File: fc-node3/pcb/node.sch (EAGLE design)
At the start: 22 parts, among them IC1 HTU21D, J1 AVR_SPI_PRG_62X3_LOCK, U1 DS18B20

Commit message: routed fc3
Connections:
- removed net DIO0: U$1.(PCINT1/AIN0/ADC1)PA1, U$4.DIO0
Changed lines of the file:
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@@
-</segment>
-</net>
-<net name="DIO0" class="0">
-<segment>
-<pinref part="U$4" gate="A" pin="DIO0"/>
-<wire x1="152.4" y1="48.26" x2="149.86" y2="48.26" width="0.1524" layer="91"/>
-<label x="149.86" y="48.26" size="1.27" layer="95" rot="R180" xref="yes"/>
-</segment>
-<segment>
-<pinref part="U$1" gate="G$1" pin="(PCINT1/AIN0/ADC1)PA1"/>
-<wire x1="45.72" y1="-58.42" x2="48.26" y2="-58.42" width="0.1524" layer="91"/>
-<label x="48.26" y="-58.42" size="1.27" layer="95" xref="yes"/>
 </segment>
 </net>

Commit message: nicey silky
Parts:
- renumbered U$2 to U2, U$3 to U3
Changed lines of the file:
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@@
 <part name="SUPPLY1" library="SparkFun-Aesthetics" deviceset="VCC" device=""/>
 <part name="GND1" library="SparkFun-Aesthetics" deviceset="GND" device=""/>
-<part name="U$2" library="ukhas" deviceset="MCP1640" device=""/>
-<part name="U$3" library="jonsowman" deviceset="BU49X_VDET_SOT235" device=""/>
+<part name="U2" library="ukhas" deviceset="MCP1640" device=""/>
+<part name="U3" library="jonsowman" deviceset="BU49X_VDET_SOT235" device=""/>
 <part name="GND2" library="SparkFun-Aesthetics" deviceset="GND" device=""/>
 <part name="GND3" library="SparkFun-Aesthetics" deviceset="GND" device=""/>
@@
 <instance part="SUPPLY1" gate="G$1" x="-7.62" y="-27.94"/>
 <instance part="GND1" gate="1" x="-7.62" y="-66.04"/>
-<instance part="U$2" gate="G$1" x="101.6" y="43.18"/>
-<instance part="U$3" gate="G$1" x="0" y="43.18"/>
+<instance part="U2" gate="G$1" x="101.6" y="43.18"/>
+<instance part="U3" gate="G$1" x="0" y="43.18"/>
 <instance part="GND2" gate="1" x="0" y="25.4"/>
 <instance part="GND3" gate="1" x="101.6" y="25.4"/>
@@
 <net name="GND" class="0">
 <segment>
-<pinref part="U$3" gate="G$1" pin="GND"/>
+<pinref part="U3" gate="G$1" pin="GND"/>
 <pinref part="GND2" gate="1" pin="GND"/>
 </segment>
 <segment>
-<pinref part="U$2" gate="G$1" pin="GND"/>
+<pinref part="U2" gate="G$1" pin="GND"/>
 <pinref part="GND3" gate="1" pin="GND"/>
 <pinref part="R2" gate="G$1" pin="1"/>
@@
 <net name="VCC" class="0">
 <segment>
-<pinref part="U$3" gate="G$1" pin="VDD"/>
+<pinref part="U3" gate="G$1" pin="VDD"/>
 <pinref part="SUPPLY2" gate="G$1" pin="VCC"/>
 </segment>
@@
 <pinref part="SUPPLY3" gate="G$1" pin="VCC"/>
 <wire x1="127" y1="50.8" x2="127" y2="48.26" width="0.1524" layer="91"/>
-<pinref part="U$2" gate="G$1" pin="VOUT"/>
+<pinref part="U2" gate="G$1" pin="VOUT"/>
 <wire x1="127" y1="48.26" x2="116.84" y2="48.26" width="0.1524" layer="91"/>
 <pinref part="R1" gate="G$1" pin="2"/>
@@
 <segment>
 <pinref part="DF" gate="G$1" pin="P$2"/>
-<pinref part="U$2" gate="G$1" pin="SW"/>
+<pinref part="U2" gate="G$1" pin="SW"/>
 <wire x1="96.52" y1="60.96" x2="101.6" y2="60.96" width="0.1524" layer="91"/>
 <wire x1="101.6" y1="60.96" x2="101.6" y2="58.42" width="0.1524" layer="91"/>
@@
 <wire x1="73.66" y1="40.64" x2="81.28" y2="40.64" width="0.1524" layer="91"/>
 <wire x1="81.28" y1="40.64" x2="81.28" y2="43.18" width="0.1524" layer="91"/>
-<pinref part="U$2" gate="G$1" pin="EN"/>
+<pinref part="U2" gate="G$1" pin="EN"/>
 <wire x1="81.28" y1="43.18" x2="86.36" y2="43.18" width="0.1524" layer="91"/>
 <pinref part="R3" gate="G$1" pin="1"/>
@@
 <pinref part="R1" gate="G$1" pin="1"/>
 <pinref part="R2" gate="G$1" pin="2"/>
-<pinref part="U$2" gate="G$1" pin="FB"/>
+<pinref part="U2" gate="G$1" pin="FB"/>
 <wire x1="116.84" y1="43.18" x2="116.84" y2="38.1" width="0.1524" layer="91"/>
 <wire x1="116.84" y1="38.1" x2="127" y2="38.1" width="0.1524" layer="91"/>
@@
 <wire x1="86.36" y1="60.96" x2="83.82" y2="60.96" width="0.1524" layer="91"/>
 <wire x1="83.82" y1="60.96" x2="83.82" y2="53.34" width="0.1524" layer="91"/>
-<pinref part="U$2" gate="G$1" pin="VIN"/>
+<pinref part="U2" gate="G$1" pin="VIN"/>
 <wire x1="83.82" y1="53.34" x2="83.82" y2="48.26" width="0.1524" layer="91"/>
 <wire x1="83.82" y1="48.26" x2="86.36" y2="48.26" width="0.1524" layer="91"/>
@@
 </segment>
 <segment>
-<pinref part="U$3" gate="G$1" pin="DETECT"/>
+<pinref part="U3" gate="G$1" pin="DETECT"/>
 <wire x1="12.7" y1="43.18" x2="15.24" y2="43.18" width="0.1524" layer="91"/>
 <label x="15.24" y="43.18" size="1.27" layer="95" xref="yes"/>

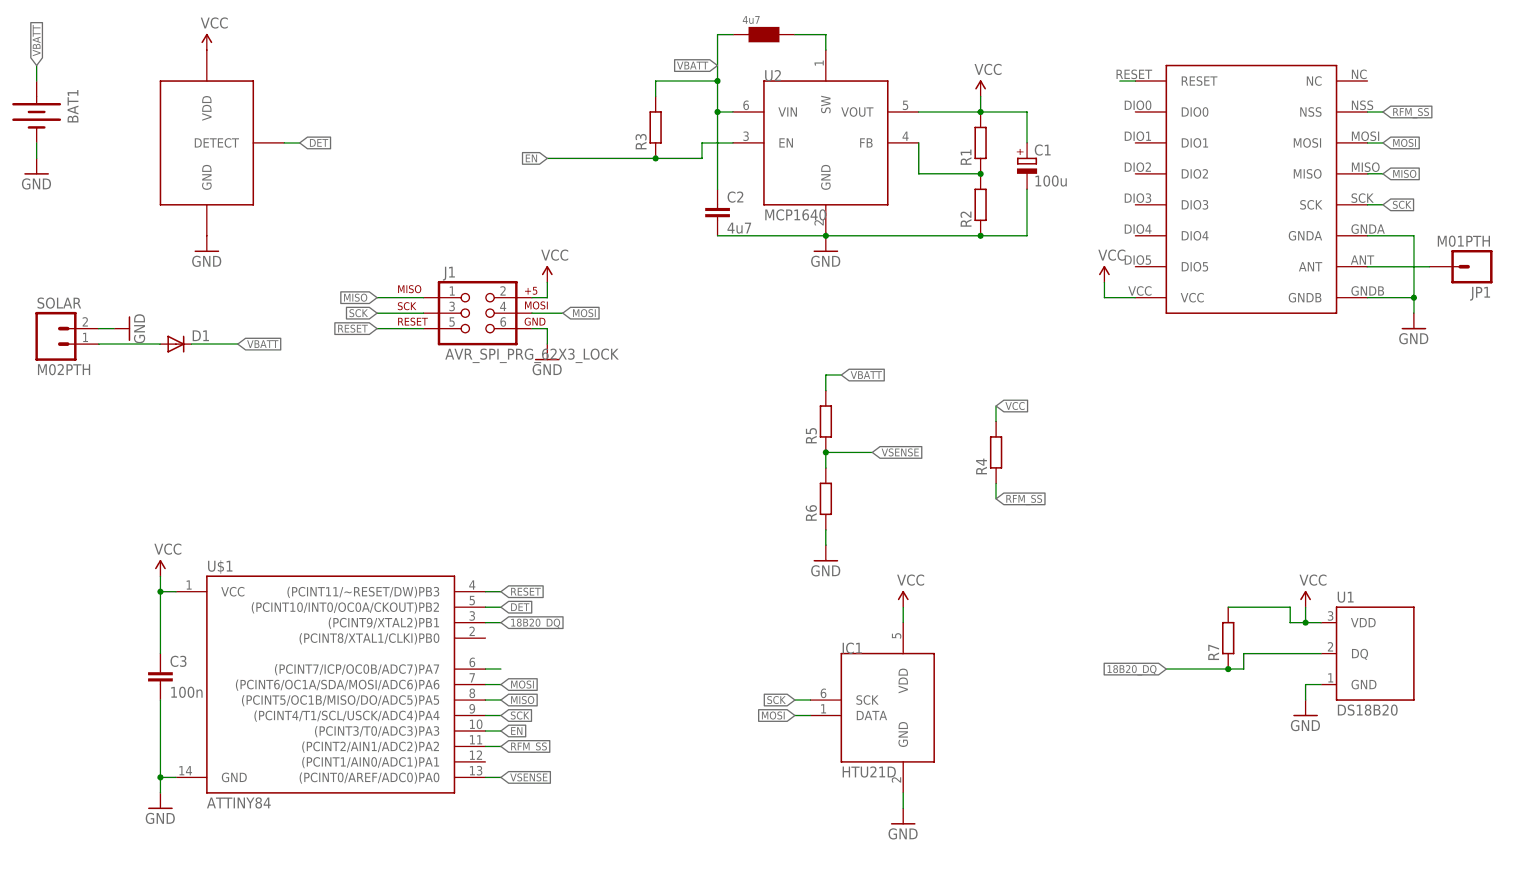
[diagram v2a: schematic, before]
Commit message: tidying routing for fc3
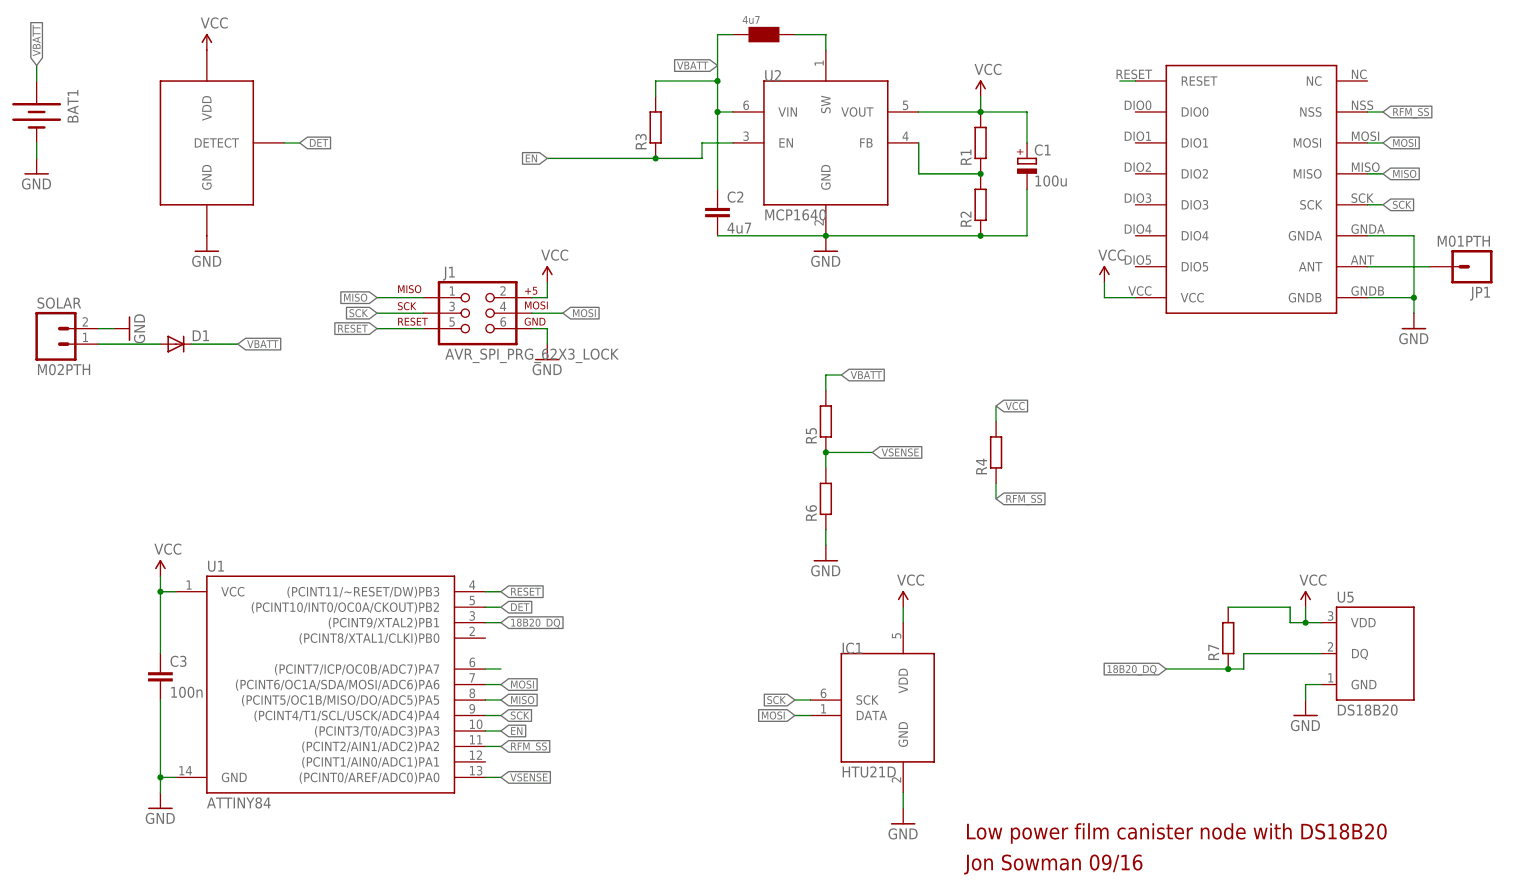
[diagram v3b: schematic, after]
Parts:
- removed U$1: ATTINY84, SparkFun-DigitalIC:ATTINY84
- added U5: DS18B20, SparkFun-Sensors:DS18B20
- U1: value DS18B20 -> ATTINY84; device SparkFun-Sensors:DS18B20 -> SparkFun-DigitalIC:ATTINY84
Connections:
- net 18B20_DQ: now also U1.(PCINT9/XTAL2)PB1, U5.DQ; no longer U$1.(PCINT9/XTAL2)PB1, U1.DQ
- net DET: now also U1.(PCINT10/INT0/OC0A/CKOUT)PB2; no longer U$1.(PCINT10/INT0/OC0A/CKOUT)PB2
- net EN: now also U1.(PCINT3/T0/ADC3)PA3; no longer U$1.(PCINT3/T0/ADC3)PA3
- net GND: now also U5.GND; no longer U$1.GND
- net MISO: now also U1.(PCINT5/OC1B/MISO/DO/ADC5)PA5; no longer U$1.(PCINT5/OC1B/MISO/DO/ADC5)PA5
- net MOSI: now also U1.(PCINT6/OC1A/SDA/MOSI/ADC6)PA6; no longer U$1.(PCINT6/OC1A/SDA/MOSI/ADC6)PA6
- net N$6: now also U1.(PCINT7/ICP/OC0B/ADC7)PA7; no longer U$1.(PCINT7/ICP/OC0B/ADC7)PA7
- net RESET: now also U1.(PCINT11/~RESET/DW)PB3; no longer U$1.(PCINT11/~RESET/DW)PB3
- net RFM_SS: now also U1.(PCINT2/AIN1/ADC2)PA2; no longer U$1.(PCINT2/AIN1/ADC2)PA2
- net SCK: now also U1.(PCINT4/T1/SCL/USCK/ADC4)PA4; no longer U$1.(PCINT4/T1/SCL/USCK/ADC4)PA4
- net VCC: now also U1.VCC, U5.VDD; no longer U$1.VCC, U1.VDD
- net VSENSE: now also U1.(PCINT0/AREF/ADC0)PA0; no longer U$1.(PCINT0/AREF/ADC0)PA0
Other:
- note added: "Jon Sowman 09/16"
- note added: "Low power film canister node with DS18B20"

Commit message: power ds18b20 from avr pin
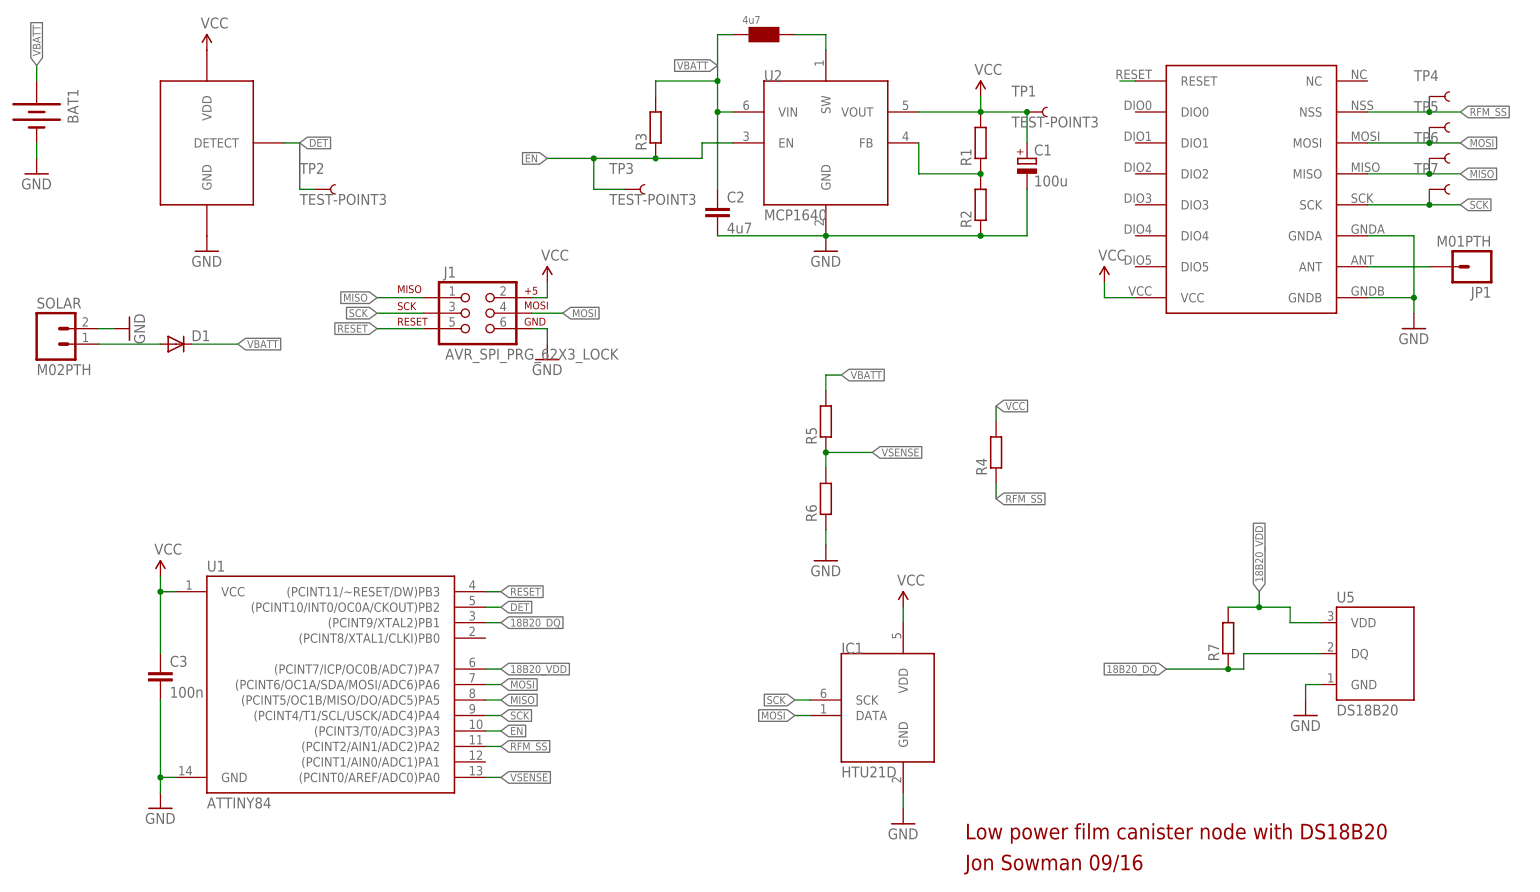
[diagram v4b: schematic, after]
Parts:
- added TP1, TP2, TP3, TP4, TP5, TP6, TP7: TEST-POINT3, SparkFun-Passives:TEST-POINT3
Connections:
- removed net N$6: U1.(PCINT7/ICP/OC0B/ADC7)PA7
- new net 18B20_VDD: R7.2, U1.(PCINT7/ICP/OC0B/ADC7)PA7, U5.VDD
- net DET: now also TP2.1
- net EN: now also TP3.1
- net MISO: now also TP6.1
- net MOSI: now also TP5.1
- net RFM_SS: now also TP4.1
- net SCK: now also TP7.1
- net VCC: now also TP1.1; no longer R7.2, U5.VDD
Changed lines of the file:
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@@
 <part name="R7" library="rcl" deviceset="R-EU_" device="R0603"/>
 <part name="GND10" library="SparkFun-Aesthetics" deviceset="GND" device=""/>
-<part name="SUPPLY7" library="SparkFun-Aesthetics" deviceset="VCC" device=""/>
+<part name="TP1" library="SparkFun-Passives" deviceset="TEST-POINT" device="3"/>
+<part name="TP2" library="SparkFun-Passives" deviceset="TEST-POINT" device="3"/>
+<part name="TP3" library="SparkFun-Passives" deviceset="TEST-POINT" device="3"/>
+<part name="TP4" library="SparkFun-Passives" deviceset="TEST-POINT" device="3"/>
+<part name="TP5" library="SparkFun-Passives" deviceset="TEST-POINT" device="3"/>
+<part name="TP6" library="SparkFun-Passives" deviceset="TEST-POINT" device="3"/>
+<part name="TP7" library="SparkFun-Passives" deviceset="TEST-POINT" device="3"/>
 </parts>
 <sheets>
@@
 <instance part="R7" gate="G$1" x="167.64" y="-38.1" rot="R90"/>
 <instance part="GND10" gate="1" x="180.34" y="-50.8"/>
-<instance part="SUPPLY7" gate="G$1" x="180.34" y="-33.02"/>
+<instance part="TP1" gate="G$1" x="134.62" y="48.26"/>
+<instance part="TP2" gate="G$1" x="17.78" y="35.56"/>
+<instance part="TP3" gate="G$1" x="68.58" y="35.56"/>
+<instance part="TP4" gate="G$1" x="200.66" y="50.8" smashed="yes">
+<attribute name="NAME" x="198.12" y="53.34" size="1.778" layer="95"/>
+</instance>
+<instance part="TP5" gate="G$1" x="200.66" y="45.72" smashed="yes">
+<attribute name="NAME" x="198.12" y="48.26" size="1.778" layer="95"/>
+</instance>
+<instance part="TP6" gate="G$1" x="200.66" y="40.64" smashed="yes">
+<attribute name="NAME" x="198.12" y="43.18" size="1.778" layer="95"/>
+</instance>
+<instance part="TP7" gate="G$1" x="200.66" y="35.56" smashed="yes">
+<attribute name="NAME" x="198.12" y="38.1" size="1.778" layer="95"/>
+</instance>
 </instances>
 <busses>
@@
 <wire x1="134.62" y1="48.26" x2="134.62" y2="43.18" width="0.1524" layer="91"/>
 <pinref part="C1" gate="G$1" pin="+"/>
+<pinref part="TP1" gate="G$1" pin="1"/>
+<junction x="134.62" y="48.26"/>
 </segment>
 <segment>
@@
 <label x="129.54" y="0" size="1.27" layer="95" font="vector" xref="yes"/>
 </segment>
-<segment>
-<pinref part="SUPPLY7" gate="G$1" pin="VCC"/>
-<wire x1="180.34" y1="-33.02" x2="180.34" y2="-35.56" width="0.1524" layer="91"/>
-<pinref part="U5" gate="G$1" pin="VDD"/>
-<wire x1="180.34" y1="-35.56" x2="182.88" y2="-35.56" width="0.1524" layer="91"/>
-<pinref part="R7" gate="G$1" pin="2"/>
-<wire x1="167.64" y1="-33.02" x2="177.8" y2="-33.02" width="0.1524" layer="91"/>
-<wire x1="177.8" y1="-33.02" x2="177.8" y2="-35.56" width="0.1524" layer="91"/>
-<wire x1="177.8" y1="-35.56" x2="180.34" y2="-35.56" width="0.1524" layer="91"/>
-<junction x="180.34" y="-35.56"/>
-</segment>
 </net>
 <net name="N$1" class="0">
@@
 <segment>
 <pinref part="U$4" gate="A" pin="MISO"/>
-<wire x1="190.5" y1="38.1" x2="193.04" y2="38.1" width="0.1524" layer="91"/>
-<label x="193.04" y="38.1" size="1.27" layer="95" font="vector" xref="yes"/>
+<wire x1="190.5" y1="38.1" x2="200.66" y2="38.1" width="0.1524" layer="91"/>
+<label x="205.74" y="38.1" size="1.27" layer="95" font="vector" xref="yes"/>
+<pinref part="TP6" gate="G$1" pin="1"/>
+<wire x1="200.66" y1="38.1" x2="205.74" y2="38.1" width="0.1524" layer="91"/>
+<wire x1="200.66" y1="40.64" x2="200.66" y2="38.1" width="0.1524" layer="91"/>
+<junction x="200.66" y="38.1"/>
 </segment>
 <segment>
@@
 <segment>
 <pinref part="U$4" gate="A" pin="MOSI"/>
-<wire x1="190.5" y1="43.18" x2="193.04" y2="43.18" width="0.1524" layer="91"/>
-<label x="193.04" y="43.18" size="1.27" layer="95" font="vector" xref="yes"/>
+<wire x1="190.5" y1="43.18" x2="200.66" y2="43.18" width="0.1524" layer="91"/>
+<label x="205.74" y="43.18" size="1.27" layer="95" font="vector" xref="yes"/>
+<pinref part="TP5" gate="G$1" pin="1"/>
+<wire x1="200.66" y1="43.18" x2="205.74" y2="43.18" width="0.1524" layer="91"/>
+<wire x1="200.66" y1="45.72" x2="200.66" y2="43.18" width="0.1524" layer="91"/>
+<junction x="200.66" y="43.18"/>
 </segment>
 <segment>
@@
 <net name="EN" class="0">
 <segment>
-<wire x1="55.88" y1="40.64" x2="73.66" y2="40.64" width="0.1524" layer="91"/>
+<wire x1="55.88" y1="40.64" x2="63.5" y2="40.64" width="0.1524" layer="91"/>
+<wire x1="63.5" y1="40.64" x2="73.66" y2="40.64" width="0.1524" layer="91"/>
 <wire x1="73.66" y1="40.64" x2="81.28" y2="40.64" width="0.1524" layer="91"/>
 <wire x1="81.28" y1="40.64" x2="81.28" y2="43.18" width="0.1524" layer="91"/>
@@
 <junction x="73.66" y="40.64"/>
 <label x="55.88" y="40.64" size="1.27" layer="95" font="vector" rot="R180" xref="yes"/>
+<pinref part="TP3" gate="G$1" pin="1"/>
+<wire x1="68.58" y1="35.56" x2="63.5" y2="35.56" width="0.1524" layer="91"/>
+<wire x1="63.5" y1="35.56" x2="63.5" y2="40.64" width="0.1524" layer="91"/>
+<junction x="63.5" y="40.64"/>
 </segment>
 <segment>
@@
 <segment>
 <pinref part="U$4" gate="A" pin="NSS"/>
-<wire x1="190.5" y1="48.26" x2="193.04" y2="48.26" width="0.1524" layer="91"/>
-<label x="193.04" y="48.26" size="1.27" layer="95" font="vector" xref="yes"/>
+<wire x1="190.5" y1="48.26" x2="200.66" y2="48.26" width="0.1524" layer="91"/>
+<label x="205.74" y="48.26" size="1.27" layer="95" font="vector" xref="yes"/>
+<pinref part="TP4" gate="G$1" pin="1"/>
+<wire x1="200.66" y1="48.26" x2="205.74" y2="48.26" width="0.1524" layer="91"/>
+<wire x1="200.66" y1="50.8" x2="200.66" y2="48.26" width="0.1524" layer="91"/>
+<junction x="200.66" y="48.26"/>
 </segment>
 <segment>
@@
 <wire x1="12.7" y1="43.18" x2="15.24" y2="43.18" width="0.1524" layer="91"/>
 <label x="15.24" y="43.18" size="1.27" layer="95" font="vector" xref="yes"/>
+<pinref part="TP2" gate="G$1" pin="1"/>
+<wire x1="17.78" y1="35.56" x2="15.24" y2="35.56" width="0.1524" layer="91"/>
+<wire x1="15.24" y1="35.56" x2="15.24" y2="43.18" width="0.1524" layer="91"/>
 </segment>
 </net>
@@
 <segment>
 <pinref part="U$4" gate="A" pin="SCK"/>
-<wire x1="190.5" y1="33.02" x2="193.04" y2="33.02" width="0.1524" layer="91"/>
-<label x="193.04" y="33.02" size="1.27" layer="95" font="vector" xref="yes"/>
+<wire x1="190.5" y1="33.02" x2="200.66" y2="33.02" width="0.1524" layer="91"/>
+<label x="205.74" y="33.02" size="1.27" layer="95" font="vector" xref="yes"/>
+<pinref part="TP7" gate="G$1" pin="1"/>
+<wire x1="200.66" y1="33.02" x2="205.74" y2="33.02" width="0.1524" layer="91"/>
+<wire x1="200.66" y1="35.56" x2="200.66" y2="33.02" width="0.1524" layer="91"/>
+<junction x="200.66" y="33.02"/>
 </segment>
 </net>
@@
 <pinref part="SOLAR" gate="G$1" pin="1"/>
 <wire x1="-17.78" y1="10.16" x2="-7.62" y2="10.16" width="0.1524" layer="91"/>
-</segment>
-</net>
-<net name="N$6" class="0">
-<segment>
-<pinref part="U1" gate="G$1" pin="(PCINT7/ICP/OC0B/ADC7)PA7"/>
-<wire x1="45.72" y1="-43.18" x2="48.26" y2="-43.18" width="0.1524" layer="91"/>
 </segment>
 </net>
@@
 </segment>
 </net>
+<net name="18B20_VDD" class="0">
+<segment>
+<pinref part="U5" gate="G$1" pin="VDD"/>
+<wire x1="180.34" y1="-35.56" x2="182.88" y2="-35.56" width="0.1524" layer="91"/>
+<pinref part="R7" gate="G$1" pin="2"/>
+<wire x1="167.64" y1="-33.02" x2="172.72" y2="-33.02" width="0.1524" layer="91"/>
+<wire x1="172.72" y1="-33.02" x2="177.8" y2="-33.02" width="0.1524" layer="91"/>
+<wire x1="177.8" y1="-33.02" x2="177.8" y2="-35.56" width="0.1524" layer="91"/>
+<wire x1="177.8" y1="-35.56" x2="180.34" y2="-35.56" width="0.1524" layer="91"/>
+<wire x1="172.72" y1="-33.02" x2="172.72" y2="-30.48" width="0.1524" layer="91"/>
+<junction x="172.72" y="-33.02"/>
+<label x="172.72" y="-30.48" size="1.27" layer="95" font="vector" rot="R90" xref="yes"/>
+</segment>
+<segment>
+<pinref part="U1" gate="G$1" pin="(PCINT7/ICP/OC0B/ADC7)PA7"/>
+<wire x1="45.72" y1="-43.18" x2="48.26" y2="-43.18" width="0.1524" layer="91"/>
+<label x="48.26" y="-43.18" size="1.27" layer="95" font="vector" xref="yes"/>
+</segment>
+</net>
